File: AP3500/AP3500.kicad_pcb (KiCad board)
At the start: 4 copper layers, 105 x 105 mm, 139 parts, among them IC2 TPS23751PWPR, J11 Barrel_Jack, J12 Bus_PCI_Express_Mini, J9 0826-1X1T-GH-F, Q1 FDS86242, U1 TPD4EUSB30, U10 TPS563249DDCR, U11 TPS563249DDCR, U12 HMHA2801AR2, U13 TPS563249DDCR, U2 TPD4EUSB30, U5 74LVC1G07SE-7, U6 TL431AIDBVR

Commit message: Almost done with new smaller AP3500 board
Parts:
- moved TP4 221.1 mm to (98.6, 22.6)
- moved C54 219.4 mm to (99.7, 37.1), turned to 0 degrees
- moved C50 216.5 mm to (91.9, 24.2), turned to 90 degrees
- moved C52 215.2 mm to (99.6, 26.5)
- moved C51 215.2 mm to (95.2, 24.2)
- moved L3 214.9 mm to (94.6, 31.3)
- moved C49 214.7 mm to (100.7, 31.6)
- moved R32 214.7 mm to (103.0, 32.1)
- moved R33 214.7 mm to (103.0, 35.1)
- moved U11 214.7 mm to (100.1, 34.1)
- moved C53 214.3 mm to (96.1, 37.1), turned to 180 degrees
- moved C55 213.6 mm to (96.3, 35.3), turned to 180 degrees
- moved R37 207.2 mm to (103.1, 49.9), turned to -90 degrees
- moved R57 206.2 mm to (91.4, 9.20), turned to 0 degrees
- moved R38 205.5 mm to (103.1, 53.0), turned to -90 degrees
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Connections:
- net /PCIE_CLK_N renamed /CM4_HighSpeed/PCIE_CLK_N
- net /PCIE_CLK_P renamed /CM4_HighSpeed/PCIE_CLK_P
- net /PCIE_CLK_nREQ renamed /CM4_HighSpeed/PCIE_CLK_nREQ
- net /PCIE_RX_N renamed /CM4_HighSpeed/PCIE_RX_N
- net /PCIE_RX_P renamed /CM4_HighSpeed/PCIE_RX_P
- net /PCIE_TX_N renamed /CM4_HighSpeed/PCIE_TX_N
- net /PCIE_TX_P renamed /CM4_HighSpeed/PCIE_TX_P
- net /PCIE_nRST renamed /CM4_HighSpeed/PCIE_nRST
- net /TR0_TAP renamed /CM4_GPIO ( Ethernet, GPIO, SDCARD)/TR0_TAP
- net /TR1_TAP renamed /CM4_GPIO ( Ethernet, GPIO, SDCARD)/TR1_TAP
- net /TR2_TAP renamed /CM4_GPIO ( Ethernet, GPIO, SDCARD)/TR2_TAP
- net /TR3_TAP renamed /CM4_GPIO ( Ethernet, GPIO, SDCARD)/TR3_TAP
- net no_connect_107 renamed no_connect_(IC2-Pad7)
- net no_connect_108 renamed no_connect_(J12-Pad10)
- net no_connect_109 renamed no_connect_(J12-Pad12)
- net no_connect_110 renamed no_connect_(J12-Pad14)
- net no_connect_111 renamed no_connect_(J12-Pad16)
- net no_connect_112 renamed no_connect_(J12-Pad17)
- net no_connect_113 renamed no_connect_(J12-Pad19)
- net no_connect_114 renamed no_connect_(J12-Pad20)
- net no_connect_115 renamed no_connect_(J12-Pad3)
- net no_connect_116 renamed no_connect_(J12-Pad30)
- net no_connect_117 renamed no_connect_(J12-Pad32)
- net no_connect_118 renamed no_connect_(J12-Pad36)
- net no_connect_119 renamed no_connect_(J12-Pad38)
- net no_connect_120 renamed no_connect_(J12-Pad42)
- net no_connect_121 renamed no_connect_(J12-Pad44)
- net no_connect_122 renamed no_connect_(J12-Pad46)
- net no_connect_123 renamed no_connect_(J12-Pad5)
- net no_connect_124 renamed no_connect_(J12-Pad8)
- net no_connect_125 renamed no_connect_(Module1-Pad100)
- net no_connect_126 renamed no_connect_(Module1-Pad101)
- net no_connect_127 renamed no_connect_(Module1-Pad103)
- net no_connect_128 renamed no_connect_(Module1-Pad104)
- net no_connect_129 renamed no_connect_(Module1-Pad105)
- net no_connect_130 renamed no_connect_(Module1-Pad106)
- net no_connect_131 renamed no_connect_(Module1-Pad111)
- net no_connect_132 renamed no_connect_(Module1-Pad115)
- net no_connect_133 renamed no_connect_(Module1-Pad117)
- net no_connect_134 renamed no_connect_(Module1-Pad121)
- net no_connect_135 renamed no_connect_(Module1-Pad123)
- net no_connect_136 renamed no_connect_(Module1-Pad127)
- net no_connect_137 renamed no_connect_(Module1-Pad128)
- net no_connect_138 renamed no_connect_(Module1-Pad129)
- net no_connect_139 renamed no_connect_(Module1-Pad130)
- net no_connect_140 renamed no_connect_(Module1-Pad133)
- net no_connect_141 renamed no_connect_(Module1-Pad134)
- net no_connect_142 renamed no_connect_(Module1-Pad135)
- net no_connect_143 renamed no_connect_(Module1-Pad136)
- net no_connect_144 renamed no_connect_(Module1-Pad139)
- net no_connect_145 renamed no_connect_(Module1-Pad140)
- net no_connect_146 renamed no_connect_(Module1-Pad141)
- net no_connect_147 renamed no_connect_(Module1-Pad142)
- net no_connect_148 renamed no_connect_(Module1-Pad143)
- net no_connect_149 renamed no_connect_(Module1-Pad145)
- net no_connect_150 renamed no_connect_(Module1-Pad146)
- net no_connect_151 renamed no_connect_(Module1-Pad147)
- net no_connect_152 renamed no_connect_(Module1-Pad148)
- net no_connect_153 renamed no_connect_(Module1-Pad149)
- net no_connect_154 renamed no_connect_(Module1-Pad151)
- net no_connect_155 renamed no_connect_(Module1-Pad152)
- net no_connect_156 renamed no_connect_(Module1-Pad153)
- net no_connect_157 renamed no_connect_(Module1-Pad154)
- net no_connect_158 renamed no_connect_(Module1-Pad157)
- net no_connect_159 renamed no_connect_(Module1-Pad158)
- net no_connect_160 renamed no_connect_(Module1-Pad159)
- net no_connect_161 renamed no_connect_(Module1-Pad16)
- net no_connect_162 renamed no_connect_(Module1-Pad160)
- net no_connect_163 renamed no_connect_(Module1-Pad163)
- net no_connect_164 renamed no_connect_(Module1-Pad164)
- net no_connect_165 renamed no_connect_(Module1-Pad165)
- net no_connect_166 renamed no_connect_(Module1-Pad166)
- net no_connect_167 renamed no_connect_(Module1-Pad169)
- net no_connect_168 renamed no_connect_(Module1-Pad170)
- net no_connect_169 renamed no_connect_(Module1-Pad171)
- net no_connect_170 renamed no_connect_(Module1-Pad172)
- net no_connect_171 renamed no_connect_(Module1-Pad175)
- net no_connect_172 renamed no_connect_(Module1-Pad176)
- net no_connect_173 renamed no_connect_(Module1-Pad177)
- net no_connect_174 renamed no_connect_(Module1-Pad178)
- net no_connect_175 renamed no_connect_(Module1-Pad18)
- net no_connect_176 renamed no_connect_(Module1-Pad181)
- net no_connect_177 renamed no_connect_(Module1-Pad182)
- net no_connect_178 renamed no_connect_(Module1-Pad183)
- net no_connect_179 renamed no_connect_(Module1-Pad184)
- net no_connect_180 renamed no_connect_(Module1-Pad187)
- net no_connect_181 renamed no_connect_(Module1-Pad188)
- net no_connect_182 renamed no_connect_(Module1-Pad189)
- net no_connect_183 renamed no_connect_(Module1-Pad19)
- net no_connect_184 renamed no_connect_(Module1-Pad190)
- net no_connect_185 renamed no_connect_(Module1-Pad193)
- net no_connect_186 renamed no_connect_(Module1-Pad194)
- net no_connect_187 renamed no_connect_(Module1-Pad195)
- net no_connect_188 renamed no_connect_(Module1-Pad196)
- net no_connect_189 renamed no_connect_(Module1-Pad199)
- net no_connect_190 renamed no_connect_(Module1-Pad200)
- net no_connect_191 renamed no_connect_(Module1-Pad35)
- net no_connect_192 renamed no_connect_(Module1-Pad36)
- net no_connect_193 renamed no_connect_(Module1-Pad57)
- net no_connect_194 renamed no_connect_(Module1-Pad61)
- net no_connect_195 renamed no_connect_(Module1-Pad62)
- net no_connect_196 renamed no_connect_(Module1-Pad63)
- net no_connect_197 renamed no_connect_(Module1-Pad64)
- net no_connect_198 renamed no_connect_(Module1-Pad67)
- net no_connect_199 renamed no_connect_(Module1-Pad68)
- net no_connect_200 renamed no_connect_(Module1-Pad69)
- net no_connect_201 renamed no_connect_(Module1-Pad70)
- net no_connect_202 renamed no_connect_(Module1-Pad72)
- net no_connect_203 renamed no_connect_(Module1-Pad73)
- net no_connect_204 renamed no_connect_(Module1-Pad75)
- net no_connect_205 renamed no_connect_(Module1-Pad76)
- net no_connect_206 renamed no_connect_(Module1-Pad80)
- net no_connect_207 renamed no_connect_(Module1-Pad82)
- net no_connect_208 renamed no_connect_(Module1-Pad84)
- net no_connect_209 renamed no_connect_(Module1-Pad86)
- net no_connect_210 renamed no_connect_(Module1-Pad88)
- net no_connect_211 renamed no_connect_(Module1-Pad89)
- net no_connect_212 renamed no_connect_(Module1-Pad90)
- net no_connect_213 renamed no_connect_(Module1-Pad91)
- net no_connect_214 renamed no_connect_(Module1-Pad92)
- net no_connect_215 renamed no_connect_(Module1-Pad93)
- net no_connect_216 renamed no_connect_(Module1-Pad94)
- net no_connect_217 renamed no_connect_(Module1-Pad96)
- net no_connect_218 renamed no_connect_(Module1-Pad97)
- net no_connect_219 renamed no_connect_(Module1-Pad99)
- H3 pad 1: GNDPWR -> GND
- H4 pad 1: GNDPWR -> GND
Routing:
- net /+3.3v: track 92.7 -> 346.5 mm, vias 22 -> 20
- net /+12v: track 4.44 -> 135.2 mm, vias 31 -> 26
- net GND: track 6.54 -> 94.8 mm, vias 90 -> 115
- net /+5v: track 20.1 -> 96.3 mm, vias 18 -> 17
- net /CM4_HighSpeed/PCIE_CLK_nREQ: track 35.1 -> 98.6 mm, vias 1 -> 2
- net /PoE/VDD: track 4.50 -> 53.4 mm, vias 0 -> 14
- net /CM4_HighSpeed/PCIE_RX_N: track 21.7 -> 65.9 mm
- net /CM4_HighSpeed/PCIE_CLK_N: track 33.6 -> 77.8 mm
- net /CM4_HighSpeed/PCIE_RX_P: track 21.8 -> 66.0 mm
- net /CM4_HighSpeed/PCIE_CLK_P: track 33.7 -> 77.8 mm
- net /CM4_HighSpeed/PCIE_TX_N: track 17.4 -> 61.0 mm
- net /CM4_HighSpeed/PCIE_TX_P: track 17.6 -> 61.0 mm
- net Net-(J9-Pad20): track 43.5 -> 3.25 mm, vias 1 -> 0
- net /CM4_HighSpeed/PCIE_nRST: track 28.8 -> 64.7 mm, vias 2 -> 0
- net /CM4_GPIO ( Ethernet, GPIO, SDCARD)/TR1_TAP: track 4.64 -> 36.7 mm
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- added copper zone on In2.Cu, net /+3.3v
- added copper zone on In1.Cu, net /PoE/VSS
- added copper zone on In2.Cu, net /PoE/VSS
- removed copper zone on In1.Cu, net /+12v
- removed copper zone on In2.Cu, net /+12v
- removed copper zone on F.Cu, net Net-(C9-Pad1)
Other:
- board text added: "12V-57V"
- board text added: "Act"
- board text added: "DC In"
- board text added: "Pwr"
- board text removed: "Activity"
- board text removed: "DC In (12v-57v)"
- board text removed: "Power"

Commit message: Finalize AP3500 board
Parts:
- removed TP1, TP11, TP4, TP5, TP6, TP7, TP9: TestPoint, TestPoint:TestPoint_Keystone_5000-5004_Miniature
- added D19: LED Green, LED_SMD:LED_0603_1608Metric, F.Cu at (73.0, 102.5)
- added D20: LED Green, LED_SMD:LED_0603_1608Metric, F.Cu at (78.0, 102.5)
- added D21: LED Green, LED_SMD:LED_0603_1608Metric, F.Cu at (83.0, 102.5)
- added D22: LED Green, LED_SMD:LED_0603_1608Metric, F.Cu at (88.0, 102.5)
- added D23: LED Green, LED_SMD:LED_0603_1608Metric, F.Cu at (93.0, 102.5)
- added D3: LED Green, LED_SMD:LED_0603_1608Metric, F.Cu at (68.0, 102.5)
- added J1: Console, Connector_PinHeader_2.54mm:PinHeader_1x04_P2.54mm_Vertical, F.Cu at (4.33, 12.8)
- added R19: 1K 1%, Resistor_SMD:R_0603_1608Metric, F.Cu at (86.2, 98.3)
- added R20: 1K 1%, Resistor_SMD:R_0603_1608Metric, F.Cu at (100.2, 96.5)
- added R36: 1K 1%, Resistor_SMD:R_0603_1608Metric, F.Cu at (100.2, 98.1)
- added R39: 1K 1%, Resistor_SMD:R_0603_1608Metric, F.Cu at (100.2, 99.8)
- added R6: 1K 1%, Resistor_SMD:R_0603_1608Metric, F.Cu at (86.2, 94.8)
- added R7: 1K 1%, Resistor_SMD:R_0603_1608Metric, F.Cu at (86.2, 96.5)
- added U3: SN74LVC07AD, Package_SO:SOIC-14_3.9x8.7mm_P1.27mm, F.Cu at (93.5, 95.4)
- moved R10 73.1 mm to (12.4, 80.1), turned to 0 degrees
- moved U5 70.5 mm to (12.3, 77.9)
- moved R1 69.8 mm to (15.6, 79.4), turned to 90 degrees
- moved D2 61.6 mm to (15.2, 84.1)
- moved D1 61.6 mm to (10.2, 84.1), turned to 0 degrees
- moved C26 3.50 mm to (88.0, 81.8)
- moved R21 3.50 mm to (90.8, 85.9)
- moved R22 3.50 mm to (88.0, 83.3)
- moved R25 3.50 mm to (88.0, 90.1)
- moved R26 3.50 mm to (88.0, 88.5)
- moved U12 3.50 mm to (82.2, 89.3)
- moved U6 3.50 mm to (91.3, 80.4)
- moved C34 3.50 mm to (91.1, 83.3)
- moved C36 3.50 mm to (85.5, 85.9)
- moved D17 3.50 mm to (88.2, 85.9)
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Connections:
- Module1 pad 51: /CM4_GPIO ( Ethernet, GPIO, SDCARD)/GPIO15 -> /CM4_GPIO ( Ethernet, GPIO, SDCARD)/UART_RX
- Module1 pad 55: /CM4_GPIO ( Ethernet, GPIO, SDCARD)/GPIO14 -> /CM4_GPIO ( Ethernet, GPIO, SDCARD)/UART_TX
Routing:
- net /CM4_GPIO ( Ethernet, GPIO, SDCARD)/GPIO22: track 0.00 -> 125.4 mm, vias 0 -> 2
- net /CM4_GPIO ( Ethernet, GPIO, SDCARD)/GPIO2: track 0.00 -> 123.4 mm, vias 0 -> 2
- net /CM4_GPIO ( Ethernet, GPIO, SDCARD)/GPIO27: track 0.00 -> 122.9 mm, vias 0 -> 2
- net /CM4_GPIO ( Ethernet, GPIO, SDCARD)/GPIO17: track 0.00 -> 122.3 mm, vias 0 -> 2
- net /CM4_GPIO ( Ethernet, GPIO, SDCARD)/GPIO3: track 0.00 -> 121.1 mm, vias 0 -> 2
- net /CM4_GPIO ( Ethernet, GPIO, SDCARD)/GPIO4: track 0.00 -> 119.5 mm, vias 0 -> 2
- net /CM4_GPIO ( Ethernet, GPIO, SDCARD)/UART_TX: track 0.00 -> 67.0 mm, vias 0 -> 2
- net /CM4_GPIO ( Ethernet, GPIO, SDCARD)/UART_RX: track 0.00 -> 63.4 mm, vias 0 -> 2
- net /+3.3v: track 346.5 -> 395.2 mm, vias 20 -> 29
- net /CM4_GPIO ( Ethernet, GPIO, SDCARD)/nPWR_LED: track 0.00 -> 46.7 mm, vias 0 -> 2
- net Net-(Module1-Pad21): track 0.00 -> 36.1 mm, vias 0 -> 2
- net Net-(D21-Pad1): track 0.00 -> 27.9 mm
- net Net-(D3-Pad1): track 0.00 -> 24.5 mm
- net /CM4_GPIO ( Ethernet, GPIO, SDCARD)/E0_LEDG: track 9.56 -> 32.8 mm
- net Net-(D22-Pad1): track 0.00 -> 19.9 mm
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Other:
- board text added: "3.3V"
- board text added: "AP3500-V2"
- board text added: "Copyright 2021 ISis ImageStream Internet Solutions, Inc."
- board text added: "GND"
- board text added: "Rx"
- board text added: "Tx"
- board text removed: "AP3500-CAM V4 r2 Copyright 2020 ISis ImageStream Internet Solutions, Inc."

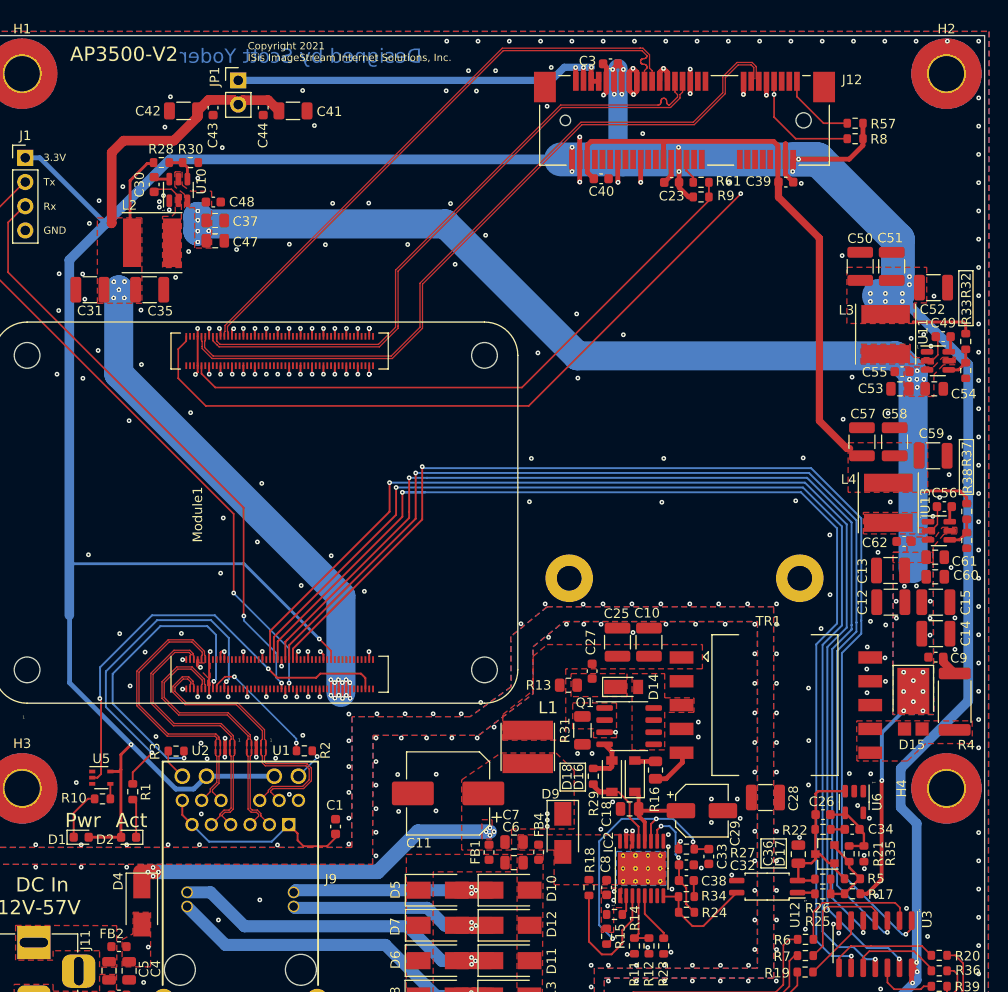
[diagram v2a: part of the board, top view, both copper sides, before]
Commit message: Placed AP3000 / AP3500 orders with JLCPCB
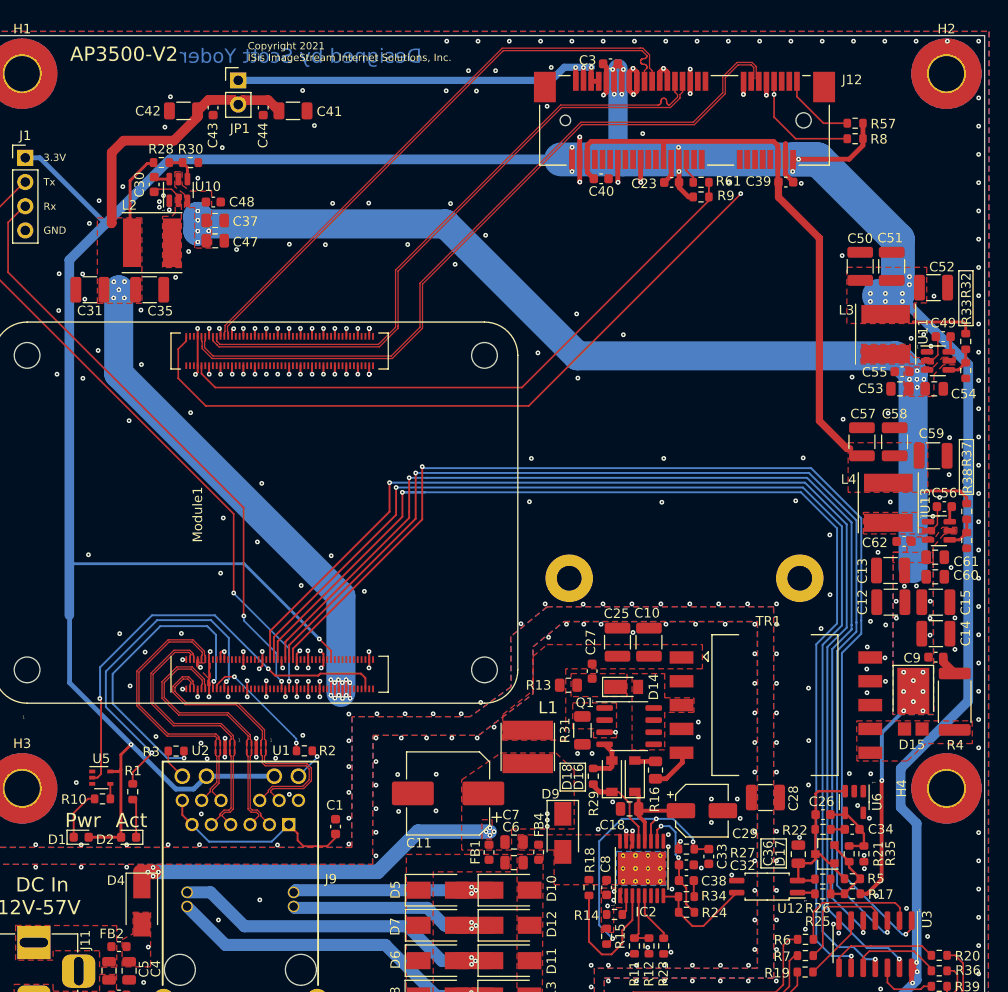
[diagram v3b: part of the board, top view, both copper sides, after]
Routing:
- net GND: track 94.7 -> 105.0 mm, vias 301 -> 312
